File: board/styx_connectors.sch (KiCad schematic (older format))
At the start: 19 parts, among them J3 Conn_01x08, J4 Styx_P4, J5 Styx_P5

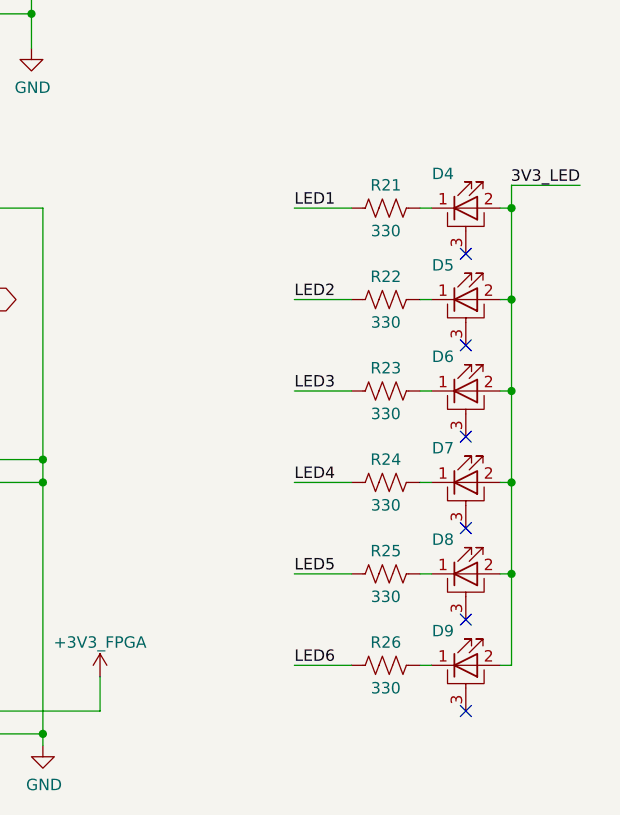
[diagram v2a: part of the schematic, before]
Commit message: Board: Reshaped and relocated some components; board may extend soon to allow a cover to neck in
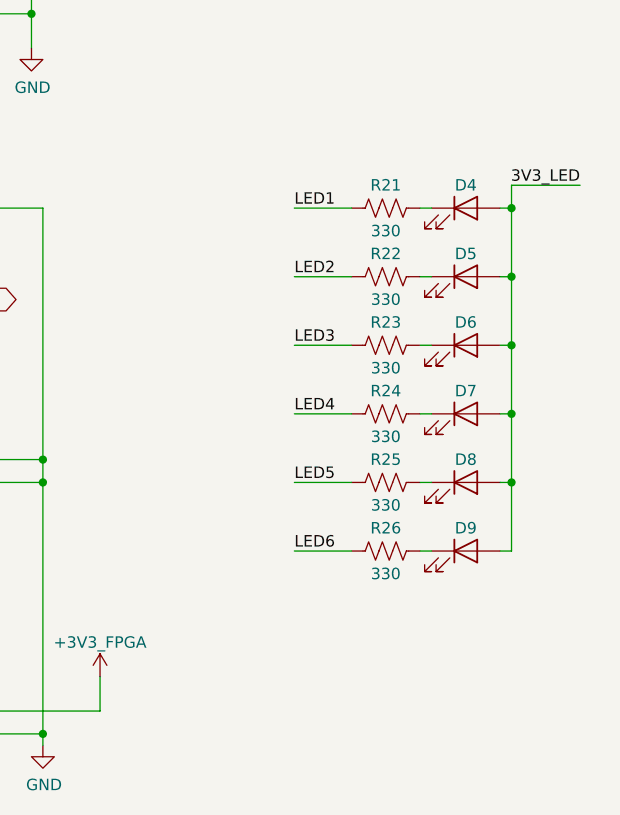
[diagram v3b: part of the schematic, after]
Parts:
- removed D4, D5, D6, D7, D8, D9: LED_PAD, agc_monitor:apa3010, symbol Device:LED_PAD
- added D4, D5, D6, D7, D8, D9: LED, LED_SMD:LED_0603_1608Metric, symbol Device:LED
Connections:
- net 3V3_LED: now also D4.2 (A), D5.2 (A), D6.2 (A), D7.2 (A), D8.2 (A), D9.2 (A)
- net at R21.1: now also D4.1 (K)
- net at R22.1: now also D5.1 (K)
- net at R23.1: now also D6.1 (K)
- net at R24.1: now also D7.1 (K)
- net at R25.1: now also D8.1 (K)
- net at R26.1: now also D9.1 (K)
- no-connect marks 22 -> 16
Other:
- moved on the sheet: R22, R23, R24, R25, R26
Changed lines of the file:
@@
 	9950 3900 9950 3800
 Wire Wire Line
-	9250 4300 9000 4300
-Text Label 9000 4300 0    50   ~ 0
+	9250 4200 9000 4200
+Text Label 9000 4200 0    50   ~ 0
 LED2
 $Comp
 L Device:R_US R22
 U 1 1 5EA444E2
-P 9400 4300
-F 0 "R22" V 9300 4300 50  0000 C CNN
-F 1 "330" V 9500 4300 50  0000 C CNN
-F 2 "Resistor_SMD:R_0603_1608Metric" V 9440 4290 50  0001 C CNN
-F 3 "~" H 9400 4300 50  0001 C CNN
-	1    9400 4300
-	0    1    1    0
-$EndComp
-Wire Wire Line
-	9600 4300 9550 4300
-Wire Wire Line
-	9950 3900 9950 4300
-Wire Wire Line
-	9950 4300 9900 4300
+P 9400 4200
+F 0 "R22" V 9300 4200 50  0000 C CNN
+F 1 "330" V 9500 4200 50  0000 C CNN
+F 2 "Resistor_SMD:R_0603_1608Metric" V 9440 4190 50  0001 C CNN
+F 3 "~" H 9400 4200 50  0001 C CNN
+	1    9400 4200
+	0    1    1    0
+$EndComp
+Wire Wire Line
+	9600 4200 9550 4200
+Wire Wire Line
+	9950 3900 9950 4200
+Wire Wire Line
+	9950 4200 9900 4200
 Connection ~ 9950 3900
 Wire Wire Line
-	9250 4700 9000 4700
-Text Label 9000 4700 0    50   ~ 0
+	9250 4500 9000 4500
+Text Label 9000 4500 0    50   ~ 0
 LED3
 $Comp
 L Device:R_US R23
 U 1 1 5EA8C987
-P 9400 4700
-F 0 "R23" V 9300 4700 50  0000 C CNN
-F 1 "330" V 9500 4700 50  0000 C CNN
-F 2 "Resistor_SMD:R_0603_1608Metric" V 9440 4690 50  0001 C CNN
-F 3 "~" H 9400 4700 50  0001 C CNN
-	1    9400 4700
-	0    1    1    0
-$EndComp
-Wire Wire Line
-	9600 4700 9550 4700
-Wire Wire Line
-	9900 4700 9950 4700
-Wire Wire Line
-	9250 5100 9000 5100
-Text Label 9000 5100 0    50   ~ 0
+P 9400 4500
+F 0 "R23" V 9300 4500 50  0000 C CNN
+F 1 "330" V 9500 4500 50  0000 C CNN
+F 2 "Resistor_SMD:R_0603_1608Metric" V 9440 4490 50  0001 C CNN
+F 3 "~" H 9400 4500 50  0001 C CNN
+	1    9400 4500
+	0    1    1    0
+$EndComp
+Wire Wire Line
+	9600 4500 9550 4500
+Wire Wire Line
+	9900 4500 9950 4500
+Wire Wire Line
+	9250 4800 9000 4800
+Text Label 9000 4800 0    50   ~ 0
 LED4
 $Comp
 L Device:R_US R24
 U 1 1 5EA8C997
-P 9400 5100
-F 0 "R24" V 9300 5100 50  0000 C CNN
-F 1 "330" V 9500 5100 50  0000 C CNN
-F 2 "Resistor_SMD:R_0603_1608Metric" V 9440 5090 50  0001 C CNN
-F 3 "~" H 9400 5100 50  0001 C CNN
-	1    9400 5100
-	0    1    1    0
-$EndComp
-Wire Wire Line
-	9600 5100 9550 5100
-Wire Wire Line
-	9950 5100 9900 5100
-Wire Wire Line
-	9950 4700 9950 4300
-Connection ~ 9950 4300
-Wire Wire Line
-	9950 5100 9950 4700
-Connection ~ 9950 4700
+P 9400 4800
+F 0 "R24" V 9300 4800 50  0000 C CNN
+F 1 "330" V 9500 4800 50  0000 C CNN
+F 2 "Resistor_SMD:R_0603_1608Metric" V 9440 4790 50  0001 C CNN
+F 3 "~" H 9400 4800 50  0001 C CNN
+	1    9400 4800
+	0    1    1    0
+$EndComp
+Wire Wire Line
+	9600 4800 9550 4800
+Wire Wire Line
+	9950 4800 9900 4800
+Wire Wire Line
+	9950 4500 9950 4200
+Connection ~ 9950 4200
+Wire Wire Line
+	9950 4800 9950 4500
+Connection ~ 9950 4500
 Wire Wire Line
 	9550 2350 9200 2350
@@
 $EndComp
 Wire Wire Line
-	9250 5500 9000 5500
-Text Label 9000 5500 0    50   ~ 0
+	9250 5100 9000 5100
+Text Label 9000 5100 0    50   ~ 0
 LED5
 $Comp
 L Device:R_US R25
 U 1 1 5E5887EB
-P 9400 5500
-F 0 "R25" V 9300 5500 50  0000 C CNN
-F 1 "330" V 9500 5500 50  0000 C CNN
-F 2 "Resistor_SMD:R_0603_1608Metric" V 9440 5490 50  0001 C CNN
-F 3 "~" H 9400 5500 50  0001 C CNN
-	1    9400 5500
-	0    1    1    0
-$EndComp
-Wire Wire Line
-	9600 5500 9550 5500
-Wire Wire Line
-	9950 5500 9900 5500
-Wire Wire Line
-	9950 5100 9950 5500
-Connection ~ 9950 5100
-Wire Wire Line
-	9250 5900 9000 5900
-Text Label 9000 5900 0    50   ~ 0
+P 9400 5100
+F 0 "R25" V 9300 5100 50  0000 C CNN
+F 1 "330" V 9500 5100 50  0000 C CNN
+F 2 "Resistor_SMD:R_0603_1608Metric" V 9440 5090 50  0001 C CNN
+F 3 "~" H 9400 5100 50  0001 C CNN
+	1    9400 5100
+	0    1    1    0
+$EndComp
+Wire Wire Line
+	9600 5100 9550 5100
+Wire Wire Line
+	9950 5100 9900 5100
+Wire Wire Line
+	9950 4800 9950 5100
+Connection ~ 9950 4800
+Wire Wire Line
+	9250 5400 9000 5400
+Text Label 9000 5400 0    50   ~ 0
 LED6
 $Comp
 L Device:R_US R26
 U 1 1 5E5B5AAF
-P 9400 5900
-F 0 "R26" V 9300 5900 50  0000 C CNN
-F 1 "330" V 9500 5900 50  0000 C CNN
-F 2 "Resistor_SMD:R_0603_1608Metric" V 9440 5890 50  0001 C CNN
-F 3 "~" H 9400 5900 50  0001 C CNN
-	1    9400 5900
-	0    1    1    0
-$EndComp
-Wire Wire Line
-	9600 5900 9550 5900
-Wire Wire Line
-	9950 5900 9900 5900
-Wire Wire Line
-	9950 5500 9950 5900
-Connection ~ 9950 5500
+P 9400 5400
+F 0 "R26" V 9300 5400 50  0000 C CNN
+F 1 "330" V 9500 5400 50  0000 C CNN
+F 2 "Resistor_SMD:R_0603_1608Metric" V 9440 5390 50  0001 C CNN
+F 3 "~" H 9400 5400 50  0001 C CNN
+	1    9400 5400
+	0    1    1    0
+$EndComp
+Wire Wire Line
+	9600 5400 9550 5400
+Wire Wire Line
+	9950 5400 9900 5400
+Wire Wire Line
+	9950 5100 9950 5400
+Connection ~ 9950 5100
 Connection ~ 5550 1250
 Wire Wire Line
@@
 $EndComp
 $Comp
-L Device:LED_PAD D4
-U 1 1 5CB34036
+L Device:LED D9
+U 1 1 5E5B5AA7
+P 9750 5400
+F 0 "D9" H 9750 5500 50  0000 C CNN
+F 1 "LED" H 9741 5525 50  0001 C CNN
+F 2 "LED_SMD:LED_0603_1608Metric" H 9750 5400 50  0001 C CNN
+F 3 "~" H 9750 5400 50  0001 C CNN
+	1    9750 5400
+	1    0    0    -1
+$EndComp
+$Comp
+L Device:LED D8
+U 1 1 5E5887E3
+P 9750 5100
+F 0 "D8" H 9750 5200 50  0000 C CNN
+F 1 "LED" H 9741 5225 50  0001 C CNN
+F 2 "LED_SMD:LED_0603_1608Metric" H 9750 5100 50  0001 C CNN
+F 3 "~" H 9750 5100 50  0001 C CNN
+	1    9750 5100
+	1    0    0    -1
+$EndComp
+$Comp
+L Device:LED D7
+U 1 1 5EA8C98F
+P 9750 4800
+F 0 "D7" H 9750 4900 50  0000 C CNN
+F 1 "LED" H 9741 4925 50  0001 C CNN
+F 2 "LED_SMD:LED_0603_1608Metric" H 9750 4800 50  0001 C CNN
+F 3 "~" H 9750 4800 50  0001 C CNN
+	1    9750 4800
+	1    0    0    -1
+$EndComp
+$Comp
+L Device:LED D6
+U 1 1 5EA8C97F
+P 9750 4500
+F 0 "D6" H 9750 4600 50  0000 C CNN
+F 1 "LED" H 9741 4625 50  0001 C CNN
+F 2 "LED_SMD:LED_0603_1608Metric" H 9750 4500 50  0001 C CNN
+F 3 "~" H 9750 4500 50  0001 C CNN
+	1    9750 4500
+	1    0    0    -1
+$EndComp
+$Comp
+L Device:LED D5
+U 1 1 5EA444DA
+P 9750 4200
+F 0 "D5" H 9750 4300 50  0000 C CNN
+F 1 "LED" H 9741 4325 50  0001 C CNN
+F 2 "LED_SMD:LED_0603_1608Metric" H 9750 4200 50  0001 C CNN
+F 3 "~" H 9750 4200 50  0001 C CNN
+	1    9750 4200
+	1    0    0    -1
+$EndComp
+$Comp
+L Device:LED D4
+U 1 1 5E9D86D0
 P 9750 3900
-F 0 "D4" H 9650 4050 50  0000 C CNN
-F 1 "LED_PAD" H 9750 4089 50  0001 C CNN
-F 2 "agc_monitor:apa3010" H 9750 3900 50  0001 C CNN
+F 0 "D4" H 9750 4000 50  0000 C CNN
+F 1 "LED" H 9741 4025 50  0001 C CNN
+F 2 "LED_SMD:LED_0603_1608Metric" H 9750 3900 50  0001 C CNN
 F 3 "~" H 9750 3900 50  0001 C CNN
 	1    9750 3900
 	1    0    0    -1
 $EndComp
-NoConn ~ 9750 4100
-$Comp
-L Device:LED_PAD D5
-U 1 1 5CBCE514
-P 9750 4300
-F 0 "D5" H 9650 4450 50  0000 C CNN
-F 1 "LED_PAD" H 9750 4489 50  0001 C CNN
-F 2 "agc_monitor:apa3010" H 9750 4300 50  0001 C CNN
-F 3 "~" H 9750 4300 50  0001 C CNN
-	1    9750 4300
-	1    0    0    -1
-$EndComp
-NoConn ~ 9750 4500
-$Comp
-L Device:LED_PAD D6
-U 1 1 5CBE4210
-P 9750 4700
-F 0 "D6" H 9650 4850 50  0000 C CNN
-F 1 "LED_PAD" H 9750 4889 50  0001 C CNN
-F 2 "agc_monitor:apa3010" H 9750 4700 50  0001 C CNN
-F 3 "~" H 9750 4700 50  0001 C CNN
-	1    9750 4700
-	1    0    0    -1
-$EndComp
-NoConn ~ 9750 4900
-$Comp
-L Device:LED_PAD D7
-U 1 1 5CBF9F4C
-P 9750 5100
-F 0 "D7" H 9650 5250 50  0000 C CNN
-F 1 "LED_PAD" H 9750 5289 50  0001 C CNN
-F 2 "agc_monitor:apa3010" H 9750 5100 50  0001 C CNN
-F 3 "~" H 9750 5100 50  0001 C CNN
-	1    9750 5100
-	1    0    0    -1
-$EndComp
-NoConn ~ 9750 5300
-$Comp
-L Device:LED_PAD D8
-U 1 1 5CBF9F53
-P 9750 5500
-F 0 "D8" H 9650 5650 50  0000 C CNN
-F 1 "LED_PAD" H 9750 5689 50  0001 C CNN
-F 2 "agc_monitor:apa3010" H 9750 5500 50  0001 C CNN
-F 3 "~" H 9750 5500 50  0001 C CNN
-	1    9750 5500
-	1    0    0    -1
-$EndComp
-NoConn ~ 9750 5700
-$Comp
-L Device:LED_PAD D9
-U 1 1 5CC0FC57
-P 9750 5900
-F 0 "D9" H 9650 6050 50  0000 C CNN
-F 1 "LED_PAD" H 9750 6089 50  0001 C CNN
-F 2 "agc_monitor:apa3010" H 9750 5900 50  0001 C CNN
-F 3 "~" H 9750 5900 50  0001 C CNN
-	1    9750 5900
-	1    0    0    -1
-$EndComp
-NoConn ~ 9750 6100
 $EndSCHEMATC

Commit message: Board: finalized v1.1 (barring any last-minute tweaks)
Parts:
- removed H10, H7, H8, H9: MountingHole, agc_monitor:MountingHole_ANSI_4, symbol Mechanical:MountingHole
- renumbered D4 to D1, D5 to D2, D6 to D3, D7 to D4, D8 to D5, D9 to D6
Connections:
- net DBG1: now also J5.12 (M22); no longer J5.15 (N19)
- net DBG2: now also J5.15 (N19); no longer J5.16 (N20)
- net DBG3: now also J5.7 (M19); no longer J5.11 (M21)
- net DBG4: now also J5.16 (N20); no longer J5.12 (M22)
- net DBG5: now also J5.8 (M20); no longer J5.7 (M19)
- net DBG6: now also J5.11 (M21); no longer J5.8 (M20)
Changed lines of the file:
@@
 LED4
 Wire Wire Line
-	6150 4000 5650 4000
-Text Label 5650 4200 0    50   ~ 0
+	7200 4000 7450 4000
+Text Label 7450 4100 2    50   ~ 0
 DBG1
 Wire Wire Line
-	7200 4000 7450 4000
-Text Label 7450 4200 2    50   ~ 0
+	6150 4100 5900 4100
+Text Label 5900 4200 0    50   ~ 0
 DBG2
 Wire Wire Line
@@
 LED6
 Wire Wire Line
-	6150 4100 5650 4100
-Text Label 5650 4100 0    50   ~ 0
+	6150 4000 5900 4000
+Text Label 5900 4000 0    50   ~ 0
 DBG3
 Wire Wire Line
-	6150 4200 5650 4200
-Text Label 5650 4000 0    50   ~ 0
+	7200 4100 7450 4100
+Text Label 7450 4000 2    50   ~ 0
 DBG5
 Wire Wire Line
-	7200 4100 7450 4100
-Text Label 7450 4100 2    50   ~ 0
+	7200 4200 7450 4200
+Text Label 7450 4200 2    50   ~ 0
 DBG4
 Wire Wire Line
-	7200 4200 7450 4200
-Text Label 7450 4000 2    50   ~ 0
+	6150 4200 5900 4200
+Text Label 5900 4100 0    50   ~ 0
 DBG6
 NoConn ~ 3750 3150
@@
 Connection ~ 4750 6100
 $Comp
-L Mechanical:MountingHole H7
-U 1 1 5C9779E4
-P 8700 850
-F 0 "H7" H 8800 896 50  0000 L CNN
-F 1 "MountingHole" H 8800 805 50  0000 L CNN
-F 2 "agc_monitor:MountingHole_ANSI_4" H 8700 850 50  0001 C CNN
-F 3 "~" H 8700 850 50  0001 C CNN
-	1    8700 850
-	1    0    0    -1
-$EndComp
-$Comp
-L Mechanical:MountingHole H8
-U 1 1 5C98D89C
-P 8700 1050
-F 0 "H8" H 8800 1096 50  0000 L CNN
-F 1 "MountingHole" H 8800 1005 50  0000 L CNN
-F 2 "agc_monitor:MountingHole_ANSI_4" H 8700 1050 50  0001 C CNN
-F 3 "~" H 8700 1050 50  0001 C CNN
-	1    8700 1050
-	1    0    0    -1
-$EndComp
-$Comp
-L Mechanical:MountingHole H9
-U 1 1 5C9A3644
-P 9550 850
-F 0 "H9" H 9650 896 50  0000 L CNN
-F 1 "MountingHole" H 9650 805 50  0000 L CNN
-F 2 "agc_monitor:MountingHole_ANSI_4" H 9550 850 50  0001 C CNN
-F 3 "~" H 9550 850 50  0001 C CNN
-	1    9550 850
-	1    0    0    -1
-$EndComp
-$Comp
-L Mechanical:MountingHole H10
-U 1 1 5C9A364A
-P 9550 1050
-F 0 "H10" H 9650 1096 50  0000 L CNN
-F 1 "MountingHole" H 9650 1005 50  0000 L CNN
-F 2 "agc_monitor:MountingHole_ANSI_4" H 9550 1050 50  0001 C CNN
-F 3 "~" H 9550 1050 50  0001 C CNN
-	1    9550 1050
-	1    0    0    -1
-$EndComp
-$Comp
-L Device:LED D9
+L Device:LED D6
 U 1 1 5E5B5AA7
 P 9750 5400
-F 0 "D9" H 9750 5500 50  0000 C CNN
+F 0 "D6" H 9750 5500 50  0000 C CNN
 F 1 "LED" H 9741 5525 50  0001 C CNN
 F 2 "LED_SMD:LED_0603_1608Metric" H 9750 5400 50  0001 C CNN
@@
 $EndComp
 $Comp
-L Device:LED D8
+L Device:LED D5
 U 1 1 5E5887E3
 P 9750 5100
-F 0 "D8" H 9750 5200 50  0000 C CNN
+F 0 "D5" H 9750 5200 50  0000 C CNN
 F 1 "LED" H 9741 5225 50  0001 C CNN
 F 2 "LED_SMD:LED_0603_1608Metric" H 9750 5100 50  0001 C CNN
@@
 $EndComp
 $Comp
-L Device:LED D7
+L Device:LED D4
 U 1 1 5EA8C98F
 P 9750 4800
-F 0 "D7" H 9750 4900 50  0000 C CNN
+F 0 "D4" H 9750 4900 50  0000 C CNN
 F 1 "LED" H 9741 4925 50  0001 C CNN
 F 2 "LED_SMD:LED_0603_1608Metric" H 9750 4800 50  0001 C CNN
@@
 $EndComp
 $Comp
-L Device:LED D6
+L Device:LED D3
 U 1 1 5EA8C97F
 P 9750 4500
-F 0 "D6" H 9750 4600 50  0000 C CNN
+F 0 "D3" H 9750 4600 50  0000 C CNN
 F 1 "LED" H 9741 4625 50  0001 C CNN
 F 2 "LED_SMD:LED_0603_1608Metric" H 9750 4500 50  0001 C CNN
@@
 $EndComp
 $Comp
-L Device:LED D5
+L Device:LED D2
 U 1 1 5EA444DA
 P 9750 4200
-F 0 "D5" H 9750 4300 50  0000 C CNN
+F 0 "D2" H 9750 4300 50  0000 C CNN
 F 1 "LED" H 9741 4325 50  0001 C CNN
 F 2 "LED_SMD:LED_0603_1608Metric" H 9750 4200 50  0001 C CNN
@@
 $EndComp
 $Comp
-L Device:LED D4
+L Device:LED D1
 U 1 1 5E9D86D0
 P 9750 3900
-F 0 "D4" H 9750 4000 50  0000 C CNN
+F 0 "D1" H 9750 4000 50  0000 C CNN
 F 1 "LED" H 9741 4025 50  0001 C CNN
 F 2 "LED_SMD:LED_0603_1608Metric" H 9750 3900 50  0001 C CNN
